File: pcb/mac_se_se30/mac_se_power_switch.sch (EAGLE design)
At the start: 7 parts, among them J1 POWER_JACKPTH

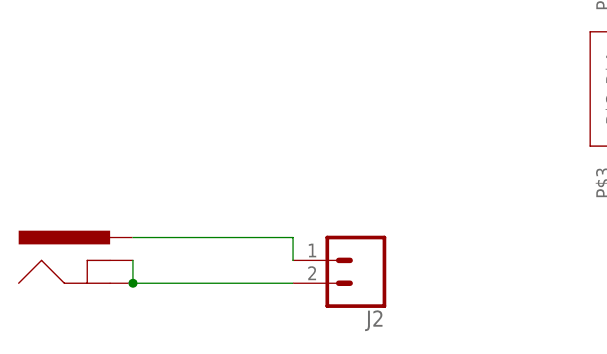
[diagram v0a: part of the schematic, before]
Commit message: updating mac SE atx adaptor
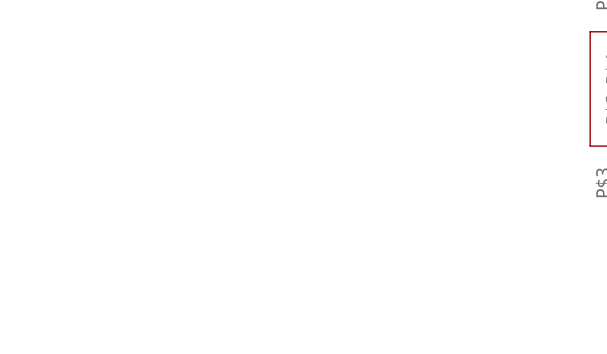
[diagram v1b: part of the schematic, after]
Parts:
- removed J1: POWER_JACKPTH, SparkFun:POWER_JACKPTH
- removed J2: (no value), atx_power_control:CONN_023.5MM-NO_SILK
- JP2: device pinhead:PINHD-1X2 -> pinhead:PINHD-1X2/90
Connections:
- removed net N$1: J1.GND, J1.GNDBREAK, J2.2
- removed net N$4: J1.PWR, J2.1
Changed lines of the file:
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@@
 <parts>
 <part name="J7" library="atx_power_control" deviceset="CONN_02" device="3.5MM-NO_SILK"/>
-<part name="JP2" library="pinhead" library_urn="urn:adsk.eagle:library:325" deviceset="PINHD-1X2" device="" package3d_urn="urn:adsk.eagle:package:22435/2"/>
+<part name="JP2" library="pinhead" library_urn="urn:adsk.eagle:library:325" deviceset="PINHD-1X2" device="/90" package3d_urn="urn:adsk.eagle:package:22437/2"/>
 <part name="U$2" library="a" deviceset="M3_MOUNTING_HOLE" device=""/>
 <part name="U$3" library="a" deviceset="M3_MOUNTING_HOLE" device=""/>
 <part name="U$1" library="atx4vc" deviceset="ROCK_SW" device=""/>
-<part name="J1" library="SparkFun" deviceset="POWER_JACK" device="PTH"/>
-<part name="J2" library="atx_power_control" deviceset="CONN_02" device="3.5MM-NO_SILK"/>
 </parts>
 <sheets>
@@
 <instance part="U$3" gate="G$1" x="-22.86" y="20.32" smashed="yes"/>
 <instance part="U$1" gate="G$1" x="-35.56" y="0" smashed="yes" rot="R90"/>
-<instance part="J1" gate="G$1" x="-96.52" y="-22.86" smashed="yes"/>
-<instance part="J2" gate="G$1" x="-68.58" y="-17.78" smashed="yes" rot="R180">
-<attribute name="VALUE" x="-66.04" y="-12.954" size="1.778" layer="96" font="vector" rot="R180"/>
-<attribute name="NAME" x="-66.04" y="-23.368" size="1.778" layer="95" font="vector" rot="R180"/>
-</instance>
 </instances>
 <busses>
@@
 </segment>
 </net>
-<net name="N$1" class="0">
-<segment>
-<pinref part="J1" gate="G$1" pin="GNDBREAK"/>
-<pinref part="J1" gate="G$1" pin="GND"/>
-<wire x1="-93.98" y1="-17.78" x2="-93.98" y2="-20.32" width="0.1524" layer="91"/>
-<pinref part="J2" gate="G$1" pin="2"/>
-<wire x1="-93.98" y1="-20.32" x2="-76.2" y2="-20.32" width="0.1524" layer="91"/>
-<junction x="-93.98" y="-20.32"/>
-</segment>
-</net>
-<net name="N$4" class="0">
-<segment>
-<pinref part="J1" gate="G$1" pin="PWR"/>
-<pinref part="J2" gate="G$1" pin="1"/>
-<wire x1="-93.98" y1="-15.24" x2="-76.2" y2="-15.24" width="0.1524" layer="91"/>
-<wire x1="-76.2" y1="-15.24" x2="-76.2" y2="-17.78" width="0.1524" layer="91"/>
-</segment>
-</net>
